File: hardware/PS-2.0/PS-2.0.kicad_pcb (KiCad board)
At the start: 2 copper layers, 119.7 x 199.4 mm, 53 parts, among them J1 PinSocket_02x16_P2.54mm_Verti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, J2 Conn_01x05, J3 Conn_01x05, J8 Conn_01x02, J9 Conn_01x02, K1 RAYEX-L90, K2 RAYEX-L90, Q1 IRFPE50, Q2 IRFPE50, Q3 IRFPE50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

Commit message: deleted:    hardware/PS-2.0/#auto_saved_files# 	deleted:    hardware/PS-2.0/PS-2.0-backups/PS-2.0-2025-08-01_153905.zip 	deleted:    hardware/PS-2.0/PS-2.0-backups/PS-2.0-2025-08-02_150037.zip 	deleted:    hardware/PS-2.0/PS-2.0-backups/PS-2.0-2025-08-05_200710.zip 	renamed:    hardware/PS-2.0/PS-2.0-backups/PS-2.0-2025-08-12_102829.zip -> hardware/PS-2.0/PS-2.0-backups/PS-2.0-2025-08-12_112522.zip 	new file:   hardware/PS-2.0/PS-2.0-backups/PS-2.0-2025-08-12_113033.zip 	new file:   hardware/PS-2.0/PS-2.0-backups/PS-2.0-2025-08-12_113628.zip 	modified:   hardware/PS-2.0/PS-2.0.kicad_pcb 	modified:   hardware/PS-2.0/PS-2.0.kicad_sch 	deleted:    hardware/XF-1.0/XF-1.0-backups/XF-1.0-2025-07-24_194858.zip 	new file:   hardware/XF-1.0/XF-1.0-backups/XF-1.0-2025-08-12_112611.zip 	modified:   pic/PS/PS2.0.png
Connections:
- J2 pad 2: (no net) -> Net-(J2-Pin_2)
- J3 pad 2: (no net) -> Net-(J3-Pin_2)
- U2 pad 6: Net-(J2-Pin_3) -> Net-(J2-Pin_2)
- U2 pad 7: Net-(J2-Pin_5) -> Net-(J2-Pin_3)
- U3 pad 6: Net-(J3-Pin_3) -> Net-(J3-Pin_2)
- U3 pad 7: Net-(J3-Pin_5) -> Net-(J3-Pin_3)
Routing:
- net Net-(J3-Pin_2): track 0.00 -> 66.3 mm
- net Net-(J3-Pin_5): track 65.1 -> 0.00 mm
- net Net-(J2-Pin_2): track 0.00 -> 25.6 mm
- net Net-(J2-Pin_5): track 24.4 -> 0.00 mm
- net Net-(J3-Pin_3): track 66.3 -> 65.1 mm
- net Net-(J2-Pin_3): track 25.6 -> 24.4 mm

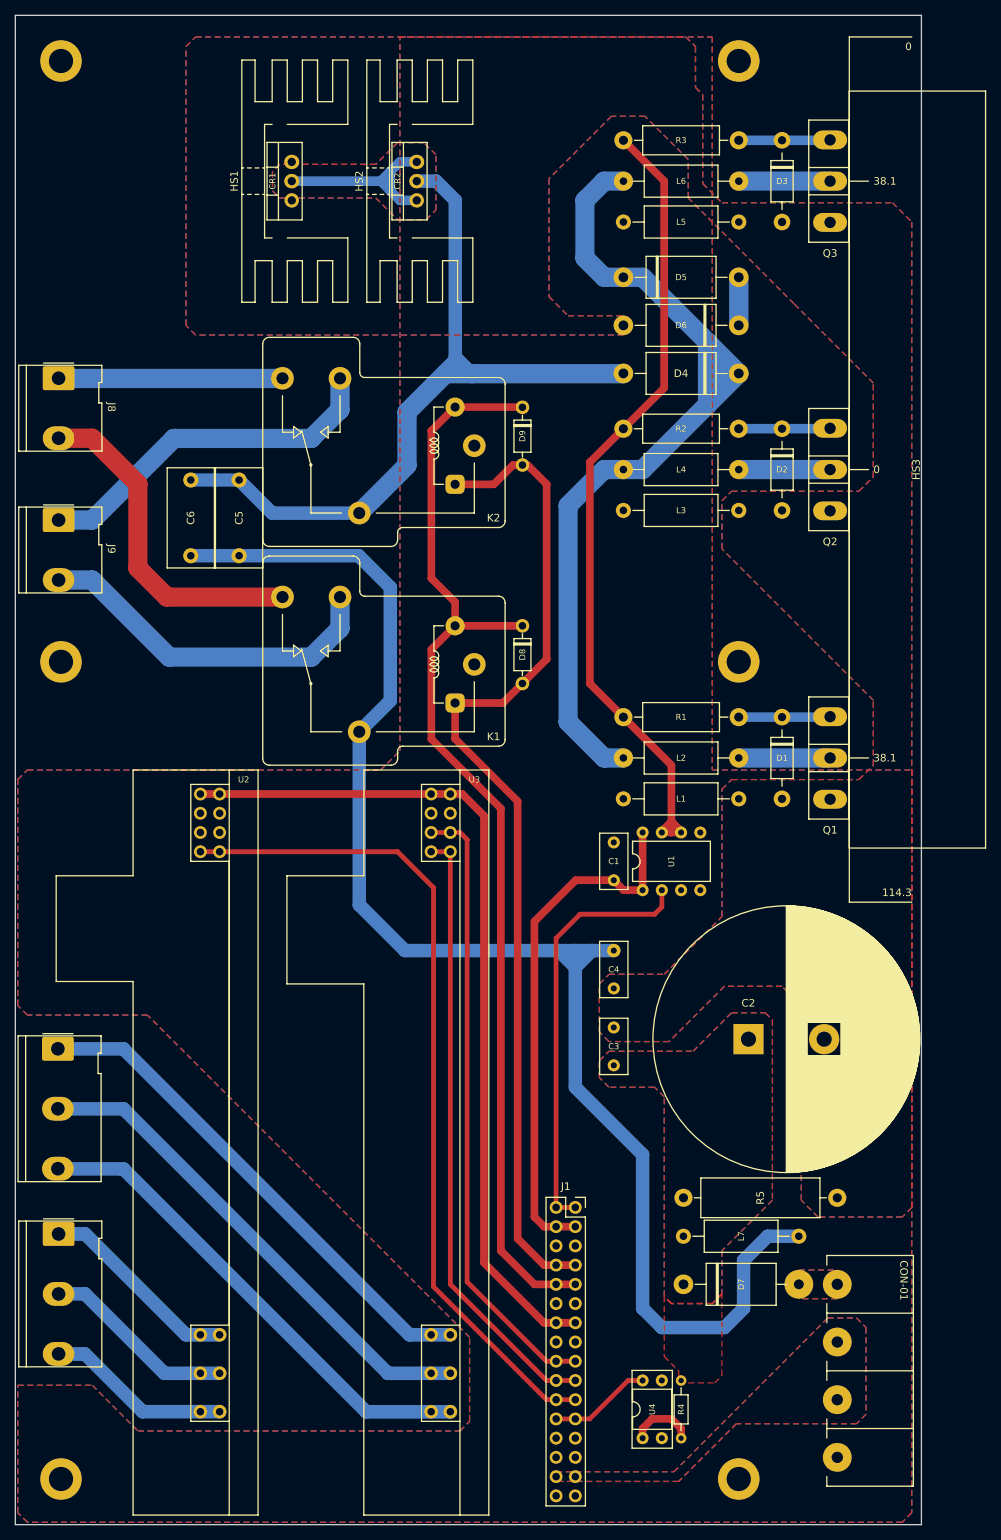
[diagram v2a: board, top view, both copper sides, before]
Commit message: modified:   .DS_Store 	modified:   Ferrite Transformer Calculation.xlsx 	modified:   README.md 	modified:   firmware/ESP32-S3 PWM/src/main.cpp 	deleted:    hardware/CTL-3.0/.~BoM.xlsx 	new file:   hardware/CTL-3.0/CTL-3.0-backups/CTL-3.0-2025-08-19_103125.zip 	new file:   hardware/CTL-4.0/BoM.xlsx 	new file:   hardware/CTL-4.0/CTL-4.0-backups/CTL-4.0-2025-08-19_120538.zip 	new file:   hardware/CTL-4.0/CTL-4.0-backups/CTL-4.0-2025-08-19_134756.zip 	new file:   hardware/CTL-4.0/CTL-4.0-backups/CTL-4.0-2025-08-19_140213.zip 	new file:   hardware/CTL-4.0/CTL-4.0-backups/CTL-4.0-2025-08-19_140737.zip 	new file:   hardware/CTL-4.0/CTL-4.0-backups/CTL-4.0-2025-08-19_153532.zip 	new file:   hardware/CTL-4.0/CTL-4.0-backups/CTL-4.0-2025-08-20_101945.zip 	new file:   hardware/CTL-4.0/CTL-4.0-backups/CTL-4.0-2025-08-22_150818.zip 	new file:   hardware/CTL-4.0/CTL-4.0.FCStd 	new file:   hardware/CTL-4.0/CTL-4.0.iges 	new file:   hardware/CTL-4.0/CTL-4.0.kicad_pcb 	new file:   hardware/CTL-4.0/CTL-4.0.kicad_prl 	new file:   hardware/CTL-4.0/CTL-4.0.kicad_pro 	new file:   hardware/CTL-4.0/CTL-4.0.kicad_sch 	new file:   hardware/CTL-4.0/CTL-4.0.png 	new file:   hardware/CTL-4.0/CTL-4.0.step 	new file:   hardware/CTL-4.0/fp-info-cache 	new file:   hardware/CTL-4.0/~CTL-4.0.kicad_sch.lck 	deleted:    hardware/PS-2.0/PS-2.0-backups/PS-2.0-2025-08-05_201831.zip 	deleted:    hardware/PS-2.0/PS-2.0-backups/PS-2.0-2025-08-05_205329.zip 	deleted:    hardware/PS-2.0/PS-2.0-backups/PS-2.0-2025-08-05_210221.zip 	deleted:    hardware/PS-2.0/PS-2.0-backups/PS-2.0-2025-08-05_211355.zip 	deleted:    hardware/PS-2.0/PS-2.0-backups/PS-2.0-2025-08-06_131643.zip 	deleted:    hardware/PS-2.0/PS-2.0-backups/PS-2.0-2025-08-06_132702.zip 	deleted:    hardware/PS-2.0/PS-2.0-backups/PS-2.0-2025-08-06_133543.zip 	new file:   hardware/PS-2.0/PS-2.0-backups/PS-2.0-2025-08-19_135413.zip 	new file:   hardware/PS-2.0/PS-2.0-backups/PS-2.0-2025-08-19_135951.zip 	new file:   hardware/PS-2.0/PS-2.0-backups/PS-2.0-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
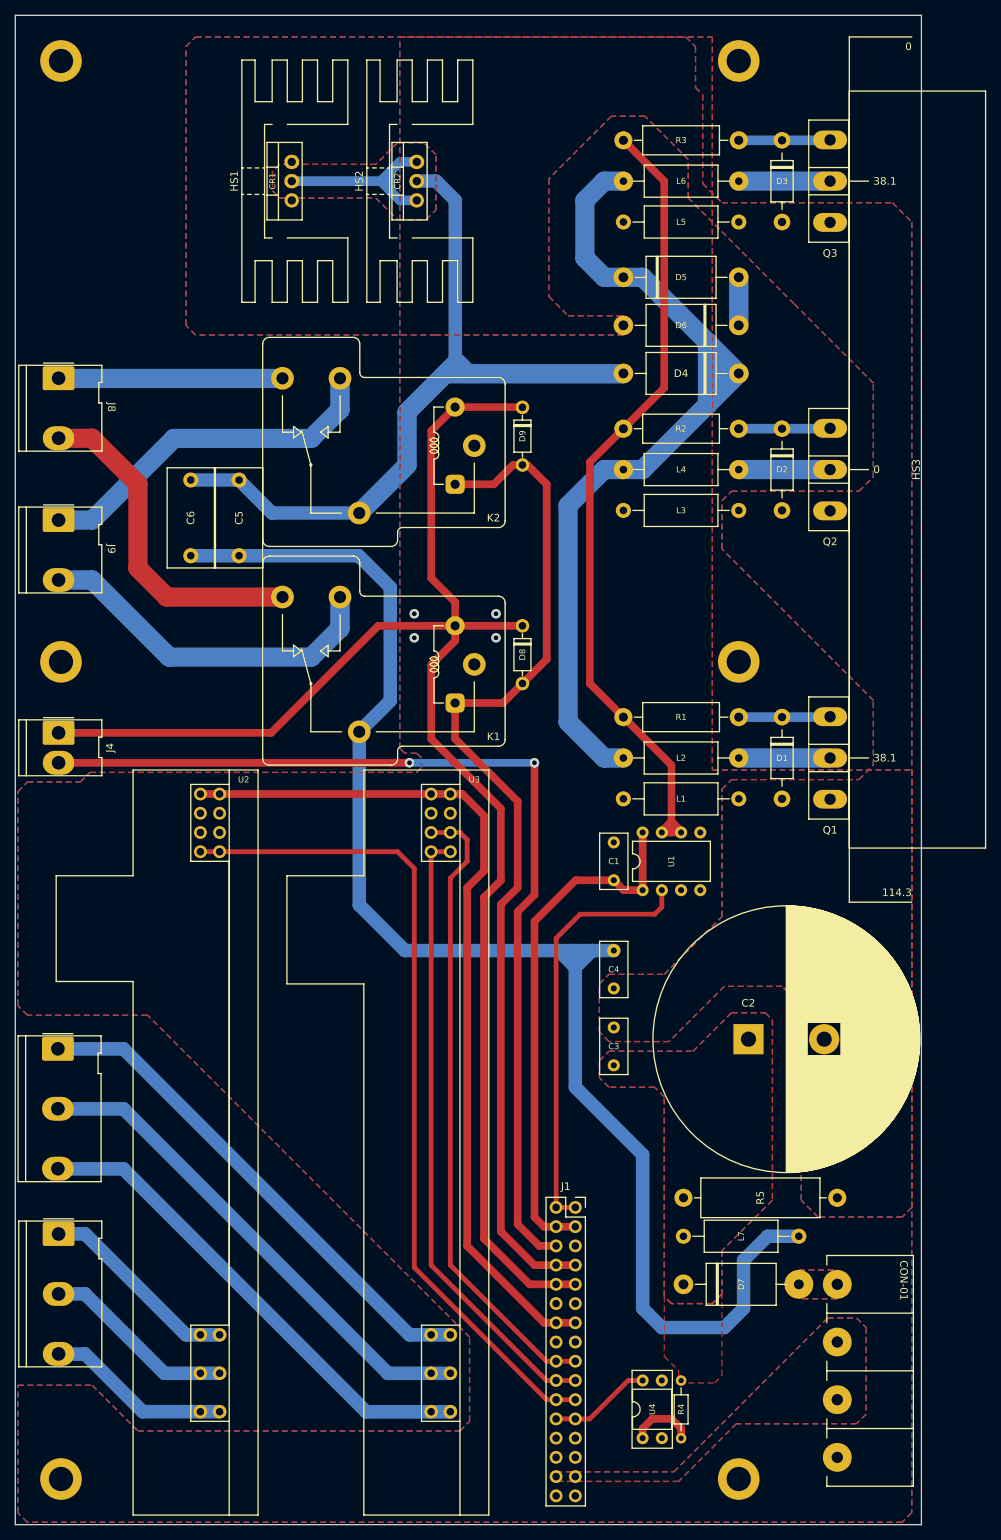
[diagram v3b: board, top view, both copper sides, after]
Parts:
- added J4: Conn_01x02, Connector_Molex:Molex_KK-396_5273-02A_1x02_P3.96mm_Vertical, F.Cu at (126.4, 124.0)
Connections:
- net /RLY-A renamed /RLY-A.1
- net Net-(C4-Pad1) renamed /OUT+
- net Net-(D4-A) renamed /OUT-
- J1 pad 3: unconnected-(J1-Pin_3-Pad3) -> /RLY-A.2
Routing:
- net /RLY-A.2: track 0.00 -> 131.0 mm, vias 0 -> 2
- net /RLY-K: track 148.0 -> 208.5 mm
- net /RLY-A.1: track 133.8 -> 136.4 mm
- net /MSD1: track 82.2 -> 84.0 mm
- net /+5V: track 113.1 -> 114.9 mm
- net /MSD2: track 81.5 -> 82.5 mm
- net GND: vias 0 -> 4
